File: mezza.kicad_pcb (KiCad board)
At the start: 2 copper layers, 85 x 54 mm, 6 parts, among them P1 CONN_02X20, P2 CONN_02X20

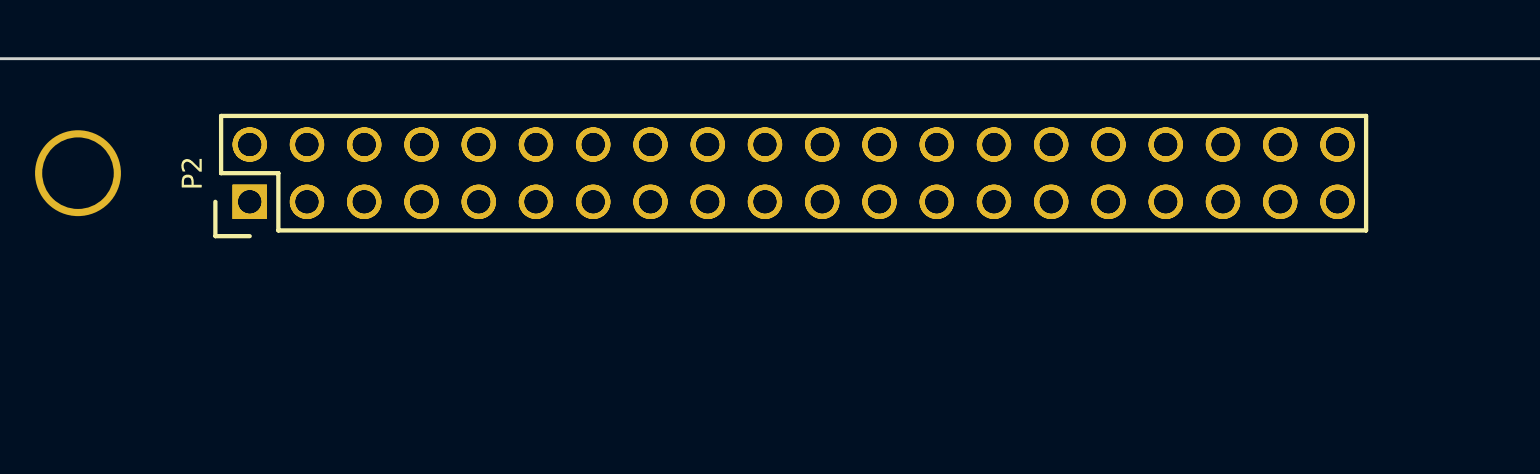
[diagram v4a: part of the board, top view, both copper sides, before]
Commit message: Flip P1/2 Board Side Placement
Looking at the 3D model, it appears that P1 (which has the socket footprint)
was attatched to the rear of the board, and P2 (which has pins) was located on
the top of the board. They have been switched round manually and realigned to
their former positions.

Signed-off-by: Sophie Haynes <sophie.haynes@linaro.org>
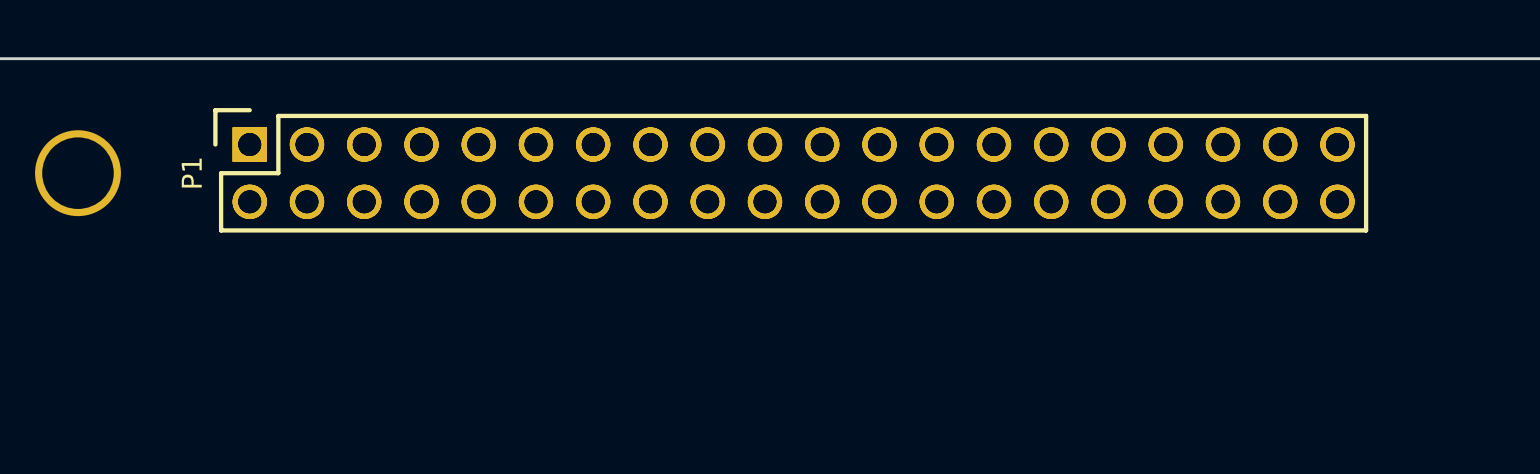
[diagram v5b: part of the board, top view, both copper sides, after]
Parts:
- P1: moved to F.Cu
- P2: moved to B.Cu
- moved P1 2.00 mm to (110.0, 103.0), turned to 90 degrees
- moved P2 2.00 mm to (110.0, 103.0), turned to 270 degrees

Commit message: Update project files
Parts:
- P1: moved to B.Cu
- P2: moved to F.Cu
- moved P1 2.00 mm to (110.0, 105.0), turned to 270 degrees
- moved P2 2.00 mm to (110.0, 105.0), turned to 90 degrees

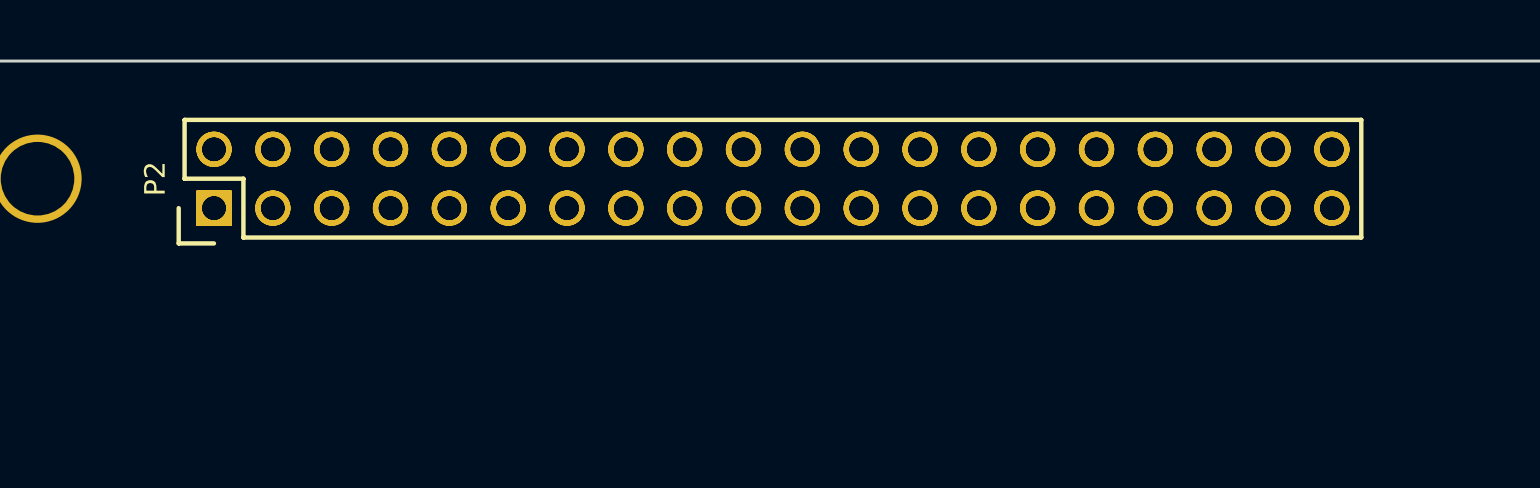
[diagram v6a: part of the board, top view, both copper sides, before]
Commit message: Default to SMD footprints on layout
Default to using SMD connectors on the layout. The user can choose to
switch to through-hole connectors if they so desire by deleting one of
the schematic objects and switching the footprint.

Signed-off-by: Grant Likely <grant.likely@linaro.org>
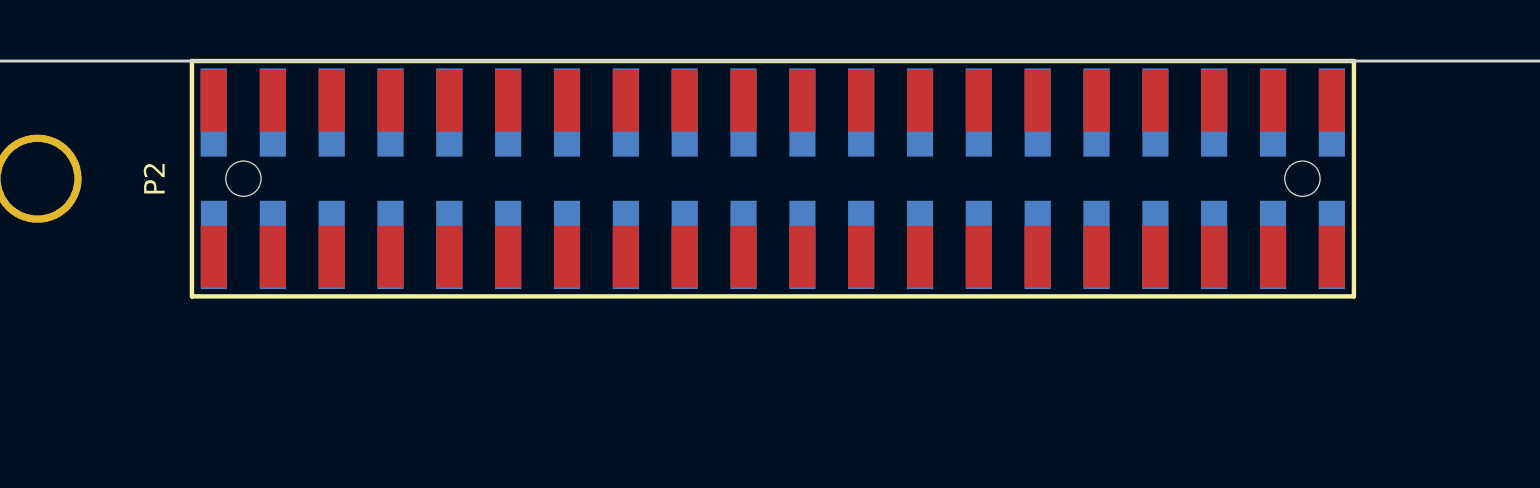
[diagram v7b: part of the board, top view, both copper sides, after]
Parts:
- P1: footprint 96boards:Pin_Header_Straight_2x20_Pitch2mm -> 96boards:Pin_Header_SMD_2x20_Pitch2mm
- P2: footprint 96boards:Socket_Strip_Straight_2x20_Pitch2mm -> 96boards:Socket_Strip_SMD_2x20_Pitch2mm
